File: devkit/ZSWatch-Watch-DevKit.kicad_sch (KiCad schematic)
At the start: 0 parts

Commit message: Update schematic and layout with KiCad 10
Co-Authored-By: Claude Opus 5.5 <noreply@anthropic.com>
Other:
- note added: "Variant: ${PCB_VARIANT}"
- note removed: "Variant: ${VARIANT}"
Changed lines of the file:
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@@
 (kicad_sch
-	(version 20250114)
+	(version 20260306)
 	(generator "eeschema")
-	(generator_version "9.0")
+	(generator_version "10.0")
 	(paper "A3")
 	(title_block
@@
 		(company "${COMPANY}")
 	)
-	(text "Variant: ${VARIANT}"
+	(text "Variant: ${PCB_VARIANT}"
 		(exclude_from_sim no)
 		(at 31.75 59.69 0)
@@
 		)
 		(fill
-			(color 0 0 0 0.0000)
+			(color 0 0 0 0)
 		)
 		(property "Sheetname" "Revision History"
 			(at 346.71 302.26 0)
+			(show_name no)
+			(do_not_autoplace no)
 			(effects
 				(font
@@
 		(property "Sheetfile" "Revision History.kicad_sch"
 			(at 347.345 304.8 0)
+			(show_name no)
+			(do_not_autoplace no)
 			(effects
 				(font
@@
 		)
 		(fill
-			(color 0 0 0 0.0000)
+			(color 0 0 0 0)
 		)
 		(property "Sheetname" "Block Diagram"
 			(at 306.07 302.5009 0)
+			(show_name no)
+			(do_not_autoplace no)
 			(effects
 				(font
@@
 		(property "Sheetfile" "Block Diagram.kicad_sch"
 			(at 307.34 304.8 0)
+			(show_name no)
+			(do_not_autoplace no)
 			(effects
 				(font
@@
 		)
 		(fill
-			(color 0 0 0 0.0000)
+			(color 0 0 0 0)
 		)
 		(property "Sheetname" "Project Architecture"
 			(at 306.07 313.9309 0)
+			(show_name no)
+			(do_not_autoplace no)
 			(effects
 				(font
@@
 		(property "Sheetfile" "Project Architecture.kicad_sch"
 			(at 307.34 316.23 0)
+			(show_name no)
+			(do_not_autoplace no)
 			(effects
 				(font
@@
 		)
 	)
-	(embedded_fonts no)
 )

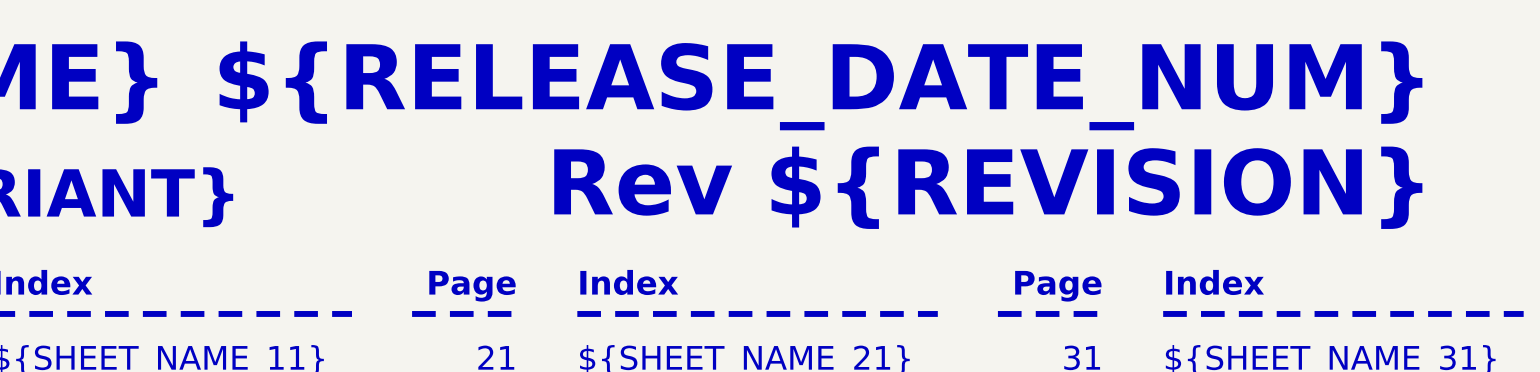
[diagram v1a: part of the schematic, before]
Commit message: Unify the project names of the schematic instances
Co-Authored-By: Claude Opus 5.5 <noreply@anthropic.com>
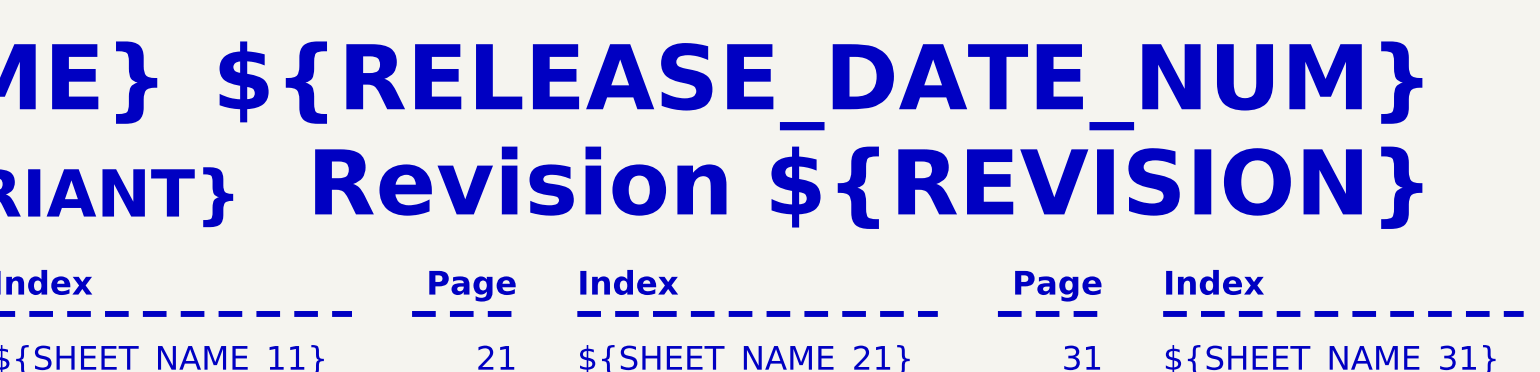
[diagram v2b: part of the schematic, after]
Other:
- note added: "Revision ${REVISION}"
- note removed: "Rev ${REVISION}"
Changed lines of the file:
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@@
 		)
 	)
-	(text "Rev ${REVISION}"
+	(text "Revision ${REVISION}"
 		(exclude_from_sim no)
 		(at 394.97 59.69 0)
@@
 		)
 	)
+	(embedded_fonts no)
 )
